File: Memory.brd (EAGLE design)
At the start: 106.7 x 37.8 mm, 8 parts, among them IC1 AT28C256ZIF, IC2 HM62256DIP

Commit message: Fix memory mapping issues
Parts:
- removed V2: 74HC00N, 74ttl-din:DIL14
- added IC3: 74LS139N, 74xx-eu:DIL16
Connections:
- removed net N$9: IC2.20, V2.3
- new net N$1: IC2.20, IC3.6
- net !MREQ: now also IC3.2; no longer V2.1, V2.10
- net A15: now also IC3.3; no longer V2.2, V2.4, V2.5, V2.6, V2.9
- net GND: now also IC3.1, IC3.8; no longer V2.7
- net N$2: now also IC3.4; no longer V2.8
- net VCC: now also IC3.16; no longer V2.14
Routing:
- net A11: track 70.7 -> 108.5 mm, vias 2 -> 1
- net A14: track 77.7 -> 40.6 mm, vias 2 -> 1
- net A15: track 103.7 -> 69.1 mm, vias 0 -> 6
- net N$9: track 32.5 -> 0.00 mm, vias 1 -> 0
- net N$1: track 0.00 -> 25.8 mm
- net A3: track 61.4 -> 80.7 mm, vias 1 -> 0
- net A13: track 80.2 -> 61.4 mm, vias 3 -> 1
- net N$2: track 124.0 -> 105.7 mm
- net D0: track 145.1 -> 130.9 mm, vias 3 -> 0
- net !MREQ: track 152.0 -> 143.0 mm
- net A1: track 71.5 -> 80.4 mm, vias 1 -> 0
- net D4: track 119.2 -> 127.8 mm
- net D1: track 102.9 -> 111.1 mm, vias 2 -> 1
- net D7: track 100.3 -> 108.4 mm, vias 2 -> 3
- net D3: track 137.8 -> 146.0 mm
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
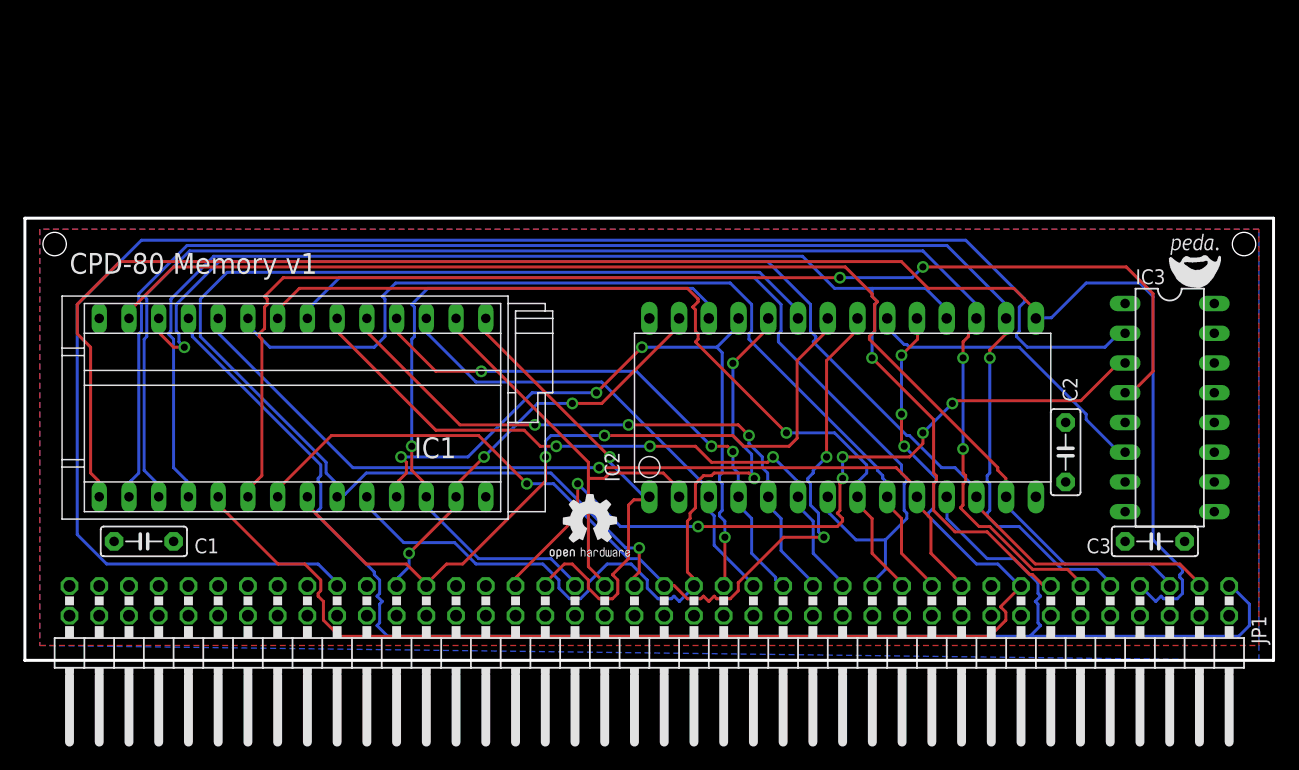
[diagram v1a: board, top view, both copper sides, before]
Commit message: Added memory ram banking to the memory board
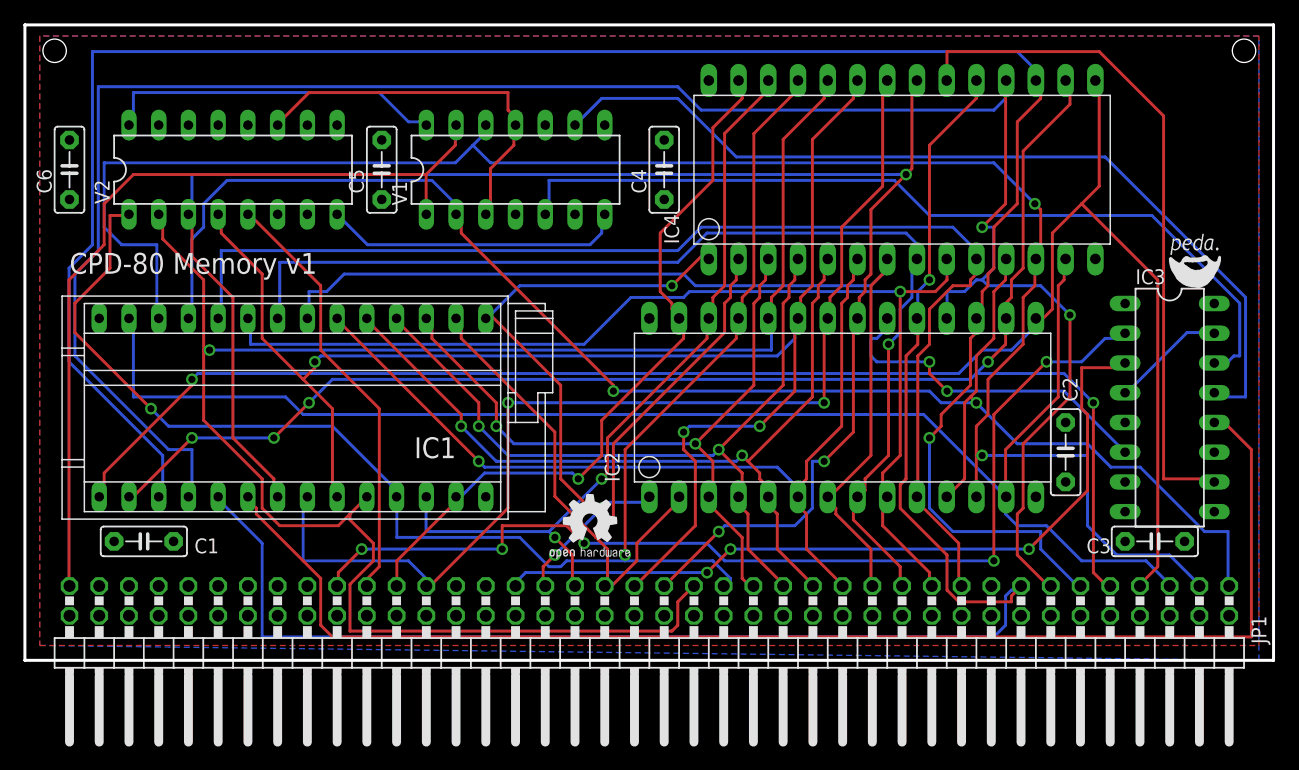
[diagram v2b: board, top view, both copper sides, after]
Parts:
- added C4, C5, C6: 0.1µF, capacitor-wima:C5B2.5
- added IC4: HM62256DIP, jean:HM62256-DIP
- added V1: 7474N, 74ttl-din:DIL14
- added V2: 74138N, 74ttl-din:DIL16
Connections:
- new net !IOREQ: JP1.59, V2.5
- new net +UB: V1.14, V2.16
- new net -UB: V1.7, V2.8
- new net N$3: IC3.14, V1.5
- new net N$4: V1.11, V1.3, V2.11
- new net N$5: IC3.13, V1.9
- new net N$6: JP1.79, V1.1, V1.13
- new net N$7: IC3.15, IC3.4
- new net N$9: IC3.10, IC4.20
- net !RD: now also IC4.22
- net !WR: now also IC4.27
- net A0: now also IC4.10
- net A1: now also IC4.9
- net A10: now also IC4.21, V2.3
- net A11: now also IC4.23, V2.4
- net A12: now also IC4.2
- net A13: now also IC4.26
- net A14: now also IC4.1
- net A2: now also IC4.8
- net A3: now also IC4.7
- net A4: now also IC4.6
- net A5: now also IC4.5
- net A6: now also IC4.4
- net A7: now also IC4.3
- net A8: now also IC4.25, V2.1
- net A9: now also IC4.24, V2.2
- net D0: now also IC4.11, V1.2
- net D1: now also IC4.12, V1.12
- net D2: now also IC4.13
- net D3: now also IC4.15
- net D4: now also IC4.16
- net D5: now also IC4.17
- net D6: now also IC4.18
- net D7: now also IC4.19
- net GND: now also C4.2, C5.2, C6.2, IC4.14, V2.6
- net N$2: now also IC3.12; no longer IC3.4
- net VCC: now also C4.1, C5.1, C6.1, IC4.28, V1.10, V1.4
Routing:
- net A9: track 67.1 -> 157.2 mm, vias 2 -> 1
- net N$5: track 0.00 -> 76.7 mm
- net N$3: track 0.00 -> 73.3 mm
- net N$6: track 0.00 -> 71.1 mm
- net A8: track 59.1 -> 129.0 mm, vias 4 -> 2
- net A10: track 79.4 -> 148.5 mm
- net D6: track 122.6 -> 181.8 mm, vias 1 -> 2
- net N$9: track 0.00 -> 58.7 mm
- net D5: track 123.8 -> 182.4 mm, vias 2 -> 1
- net !MREQ: track 143.0 -> 87.9 mm, vias 0 -> 5
- net D1: track 111.1 -> 156.5 mm, vias 1 -> 2
- net !IOREQ: track 0.00 -> 36.9 mm
- net N$4: track 0.00 -> 32.5 mm
- net A12: track 37.5 -> 68.2 mm
- net A0: track 76.4 -> 105.8 mm, vias 1 -> 0
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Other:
- board size 106.7 x 37.8 mm -> 106.7 x 54.3 mm

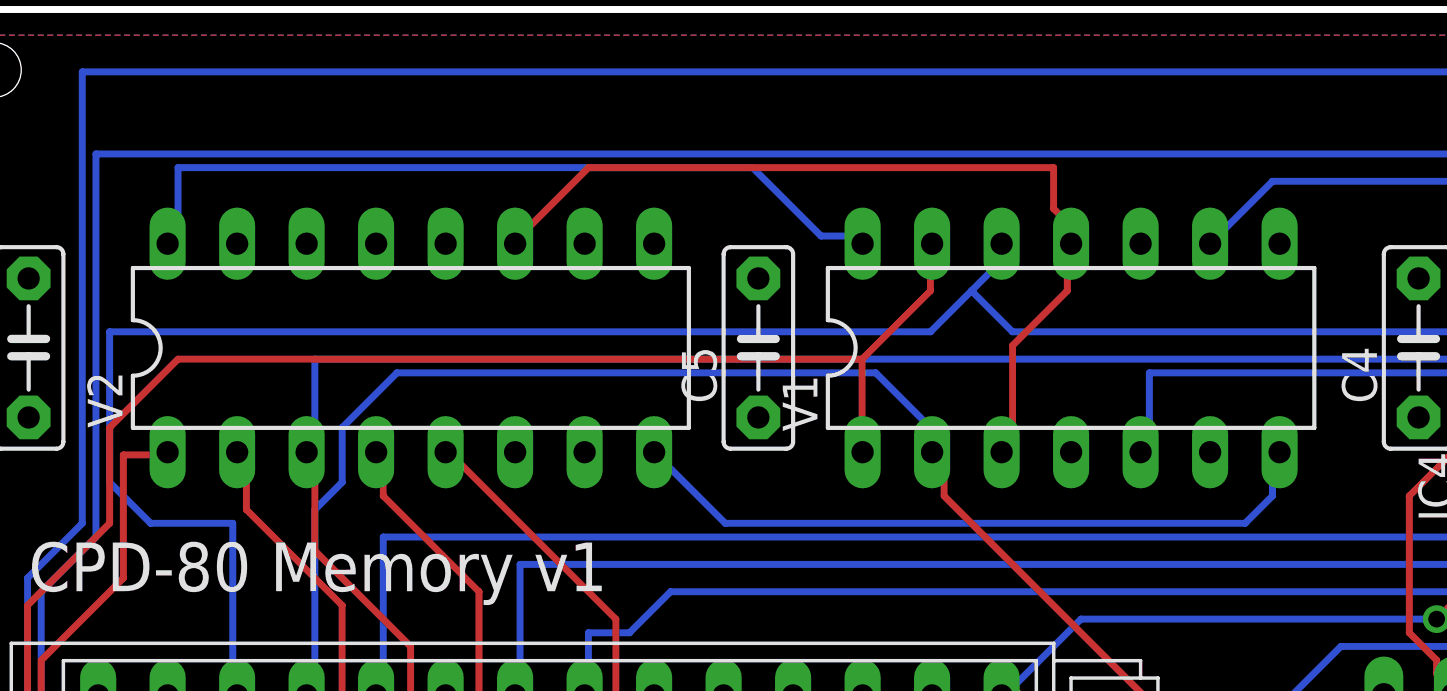
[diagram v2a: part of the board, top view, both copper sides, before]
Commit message: Fix Missing VCC and GND Connections
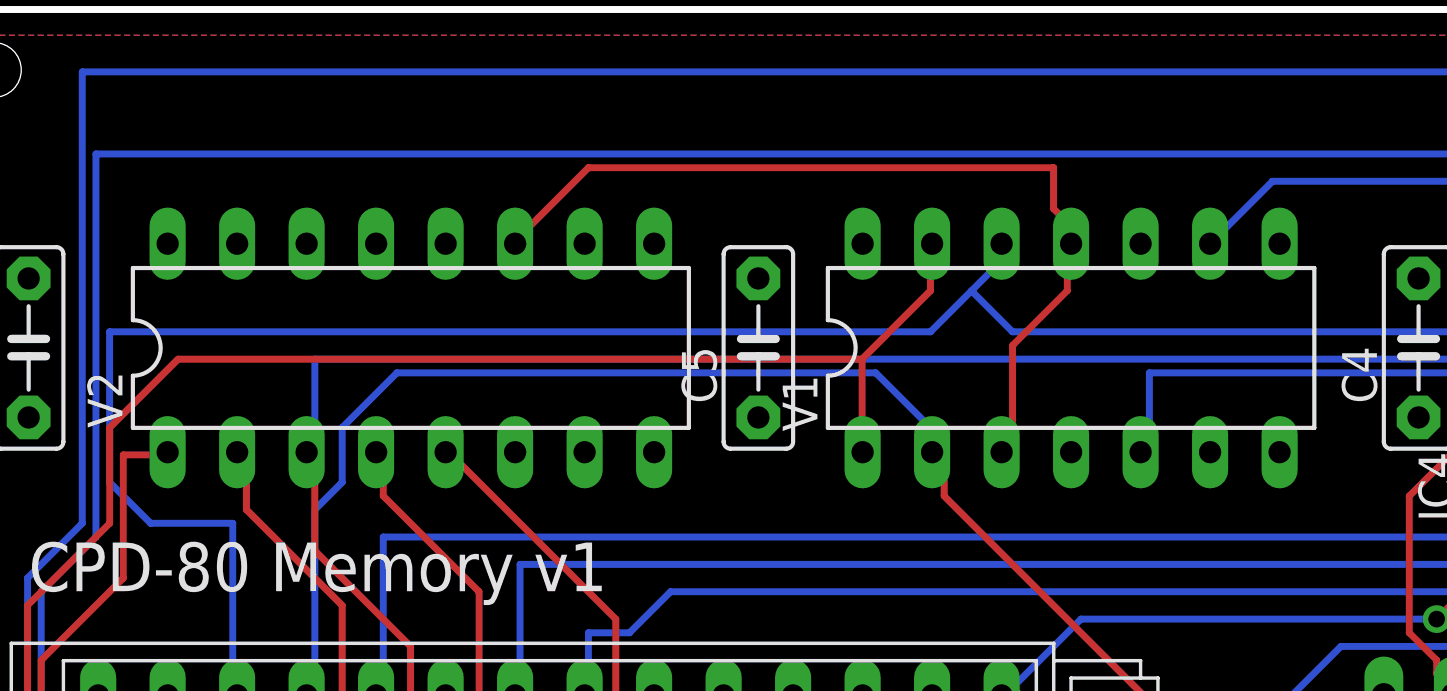
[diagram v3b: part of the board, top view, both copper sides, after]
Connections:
- removed net +UB: V1.14, V2.16
- removed net -UB: V1.7, V2.8
- net GND: now also V1.7, V2.8
- net VCC: now also V1.14, V2.16
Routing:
- net +UB: track 29.3 -> 0.00 mm
- net -UB: track 25.9 -> 0.00 mm
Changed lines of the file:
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@@
 <contactref element="C5" pad="1"/>
 <contactref element="C6" pad="1"/>
+<contactref element="V2" pad="16"/>
+<contactref element="V1" pad="14"/>
 <wire x1="87.63" y1="15.24" x2="92.71" y2="10.16" width="0" layer="19" extent="1-1"/>
 <wire x1="38.1" y1="13.97" x2="52.07" y2="29.21" width="0" layer="19" extent="1-1"/>
@@
 <contactref element="C5" pad="2"/>
 <contactref element="C6" pad="2"/>
+<contactref element="V2" pad="8"/>
+<contactref element="V1" pad="7"/>
 <wire x1="85.09" y1="13.97" x2="92.71" y2="12.7" width="0" layer="19" extent="1-1"/>
 <wire x1="87.63" y1="20.32" x2="85.09" y2="13.97" width="0" layer="19" extent="1-1"/>
 <wire x1="5.08" y1="29.21" x2="2.54" y2="44.45" width="0" layer="19" extent="1-1"/>
-<wire x1="29.21" y1="44.45" x2="20.32" y2="38.1" width="0" layer="19" extent="1-1"/>
+<wire x1="29.21" y1="44.45" x2="25.4" y2="38.1" width="0" layer="19" extent="1-1"/>
 </signal>
 <signal name="!MREQ">
@@
 <via x="76" y="25.5" extent="1-16" drill="0.6096"/>
 </signal>
-<signal name="+UB">
-<contactref element="V1" pad="14"/>
-<contactref element="V2" pad="16"/>
-<wire x1="8" y1="48.5" x2="8" y2="46" width="0.254" layer="16"/>
-<wire x1="29" y1="48.5" x2="8" y2="48.5" width="0.254" layer="16"/>
-<wire x1="31.5" y1="46" x2="29" y2="48.5" width="0.254" layer="16"/>
-<wire x1="33" y1="46" x2="31.5" y2="46" width="0.254" layer="16"/>
-<wire x1="8" y1="46" x2="7.62" y2="45.72" width="0.254" layer="16"/>
-<wire x1="33" y1="46" x2="33.02" y2="45.72" width="0.254" layer="16"/>
-</signal>
-<signal name="-UB">
-<contactref element="V1" pad="7"/>
-<contactref element="V2" pad="8"/>
-<wire x1="28" y1="35.5" x2="25.4" y2="38.1" width="0.254" layer="16"/>
-<wire x1="47" y1="35.5" x2="28" y2="35.5" width="0.254" layer="16"/>
-<wire x1="48" y1="36.5" x2="47" y2="35.5" width="0.254" layer="16"/>
-<wire x1="48" y1="38" x2="48" y2="36.5" width="0.254" layer="16"/>
-<wire x1="48" y1="38" x2="48.26" y2="38.1" width="0.254" layer="16"/>
-</signal>
 <signal name="!IOREQ">

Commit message: Update Memory
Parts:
- moved C6 90.6 mm to (92.7, 33.0)
- moved V2 62.9 mm to (78.7, 33.0)
- moved C5 59.7 mm to (88.9, 44.5)
- moved IC4 52.7 mm to (15.2, 22.9), turned to 90 degrees
- moved C2 44.5 mm to (43.2, 19.1), turned to 270 degrees
- moved C4 39.9 mm to (29.2, 10.2), turned to 180 degrees
- moved V1 36.9 mm to (77.5, 44.5)
- moved IC1 35.4 mm to (55.9, 30.5), turned to 90 degrees
- moved IC2 25.0 mm to (36.8, 22.9), turned to 90 degrees
- moved U$1 22.9 mm to (66.0, 6.35)
- moved IC3 17.8 mm to (78.7, 20.3), turned to 0 degrees
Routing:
- net N$1: track 29.9 -> 118.9 mm, vias 2 -> 1
- net N$9: track 58.7 -> 133.5 mm, vias 0 -> 1
- net N$2: track 113.6 -> 38.8 mm
- net D6: track 181.8 -> 121.4 mm
- net A9: track 157.2 -> 99.6 mm, vias 1 -> 2
- net N$3: track 73.3 -> 19.2 mm
- net !IOREQ: track 36.9 -> 89.0 mm
- net N$6: track 71.1 -> 119.3 mm, vias 0 -> 1
- net D5: track 182.4 -> 136.9 mm
- net N$5: track 76.7 -> 37.9 mm
- net A8: track 129.0 -> 100.2 mm, vias 2 -> 1
- net A10: track 148.5 -> 120.0 mm, vias 3 -> 1
- net D1: track 156.5 -> 128.5 mm, vias 2 -> 0
- net A15: track 67.2 -> 42.8 mm, vias 3 -> 1
- net A11: track 129.8 -> 107.2 mm, vias 3 -> 0
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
